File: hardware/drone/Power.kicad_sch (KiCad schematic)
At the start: 73 parts, among them Q1 ISP650P06NM, U1 STM32N645I0, U13 LM5907, U16 LMR51635XFDDCR, U18 TPS2121, U3 TPS628303, U4 TPS7A2118PQWDSGRQ1, U5 TPS628303

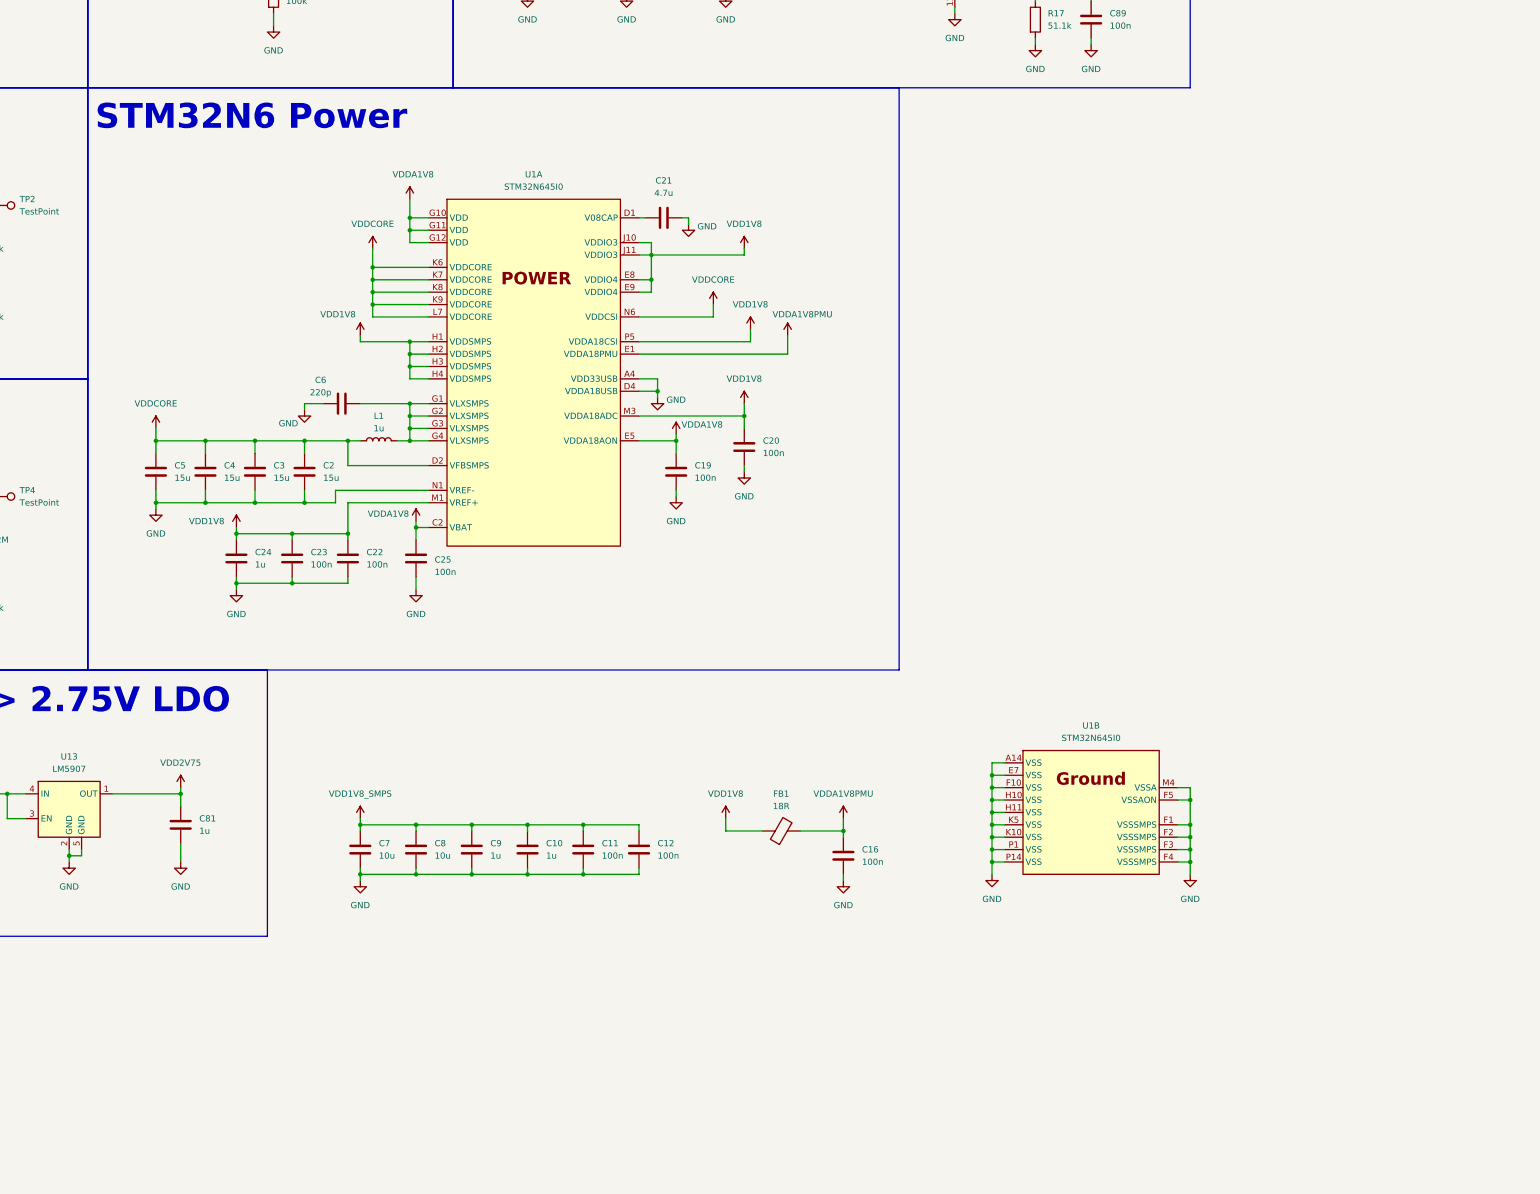
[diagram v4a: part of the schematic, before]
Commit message: Finished MCU schematic decoupling, finished system control schematic
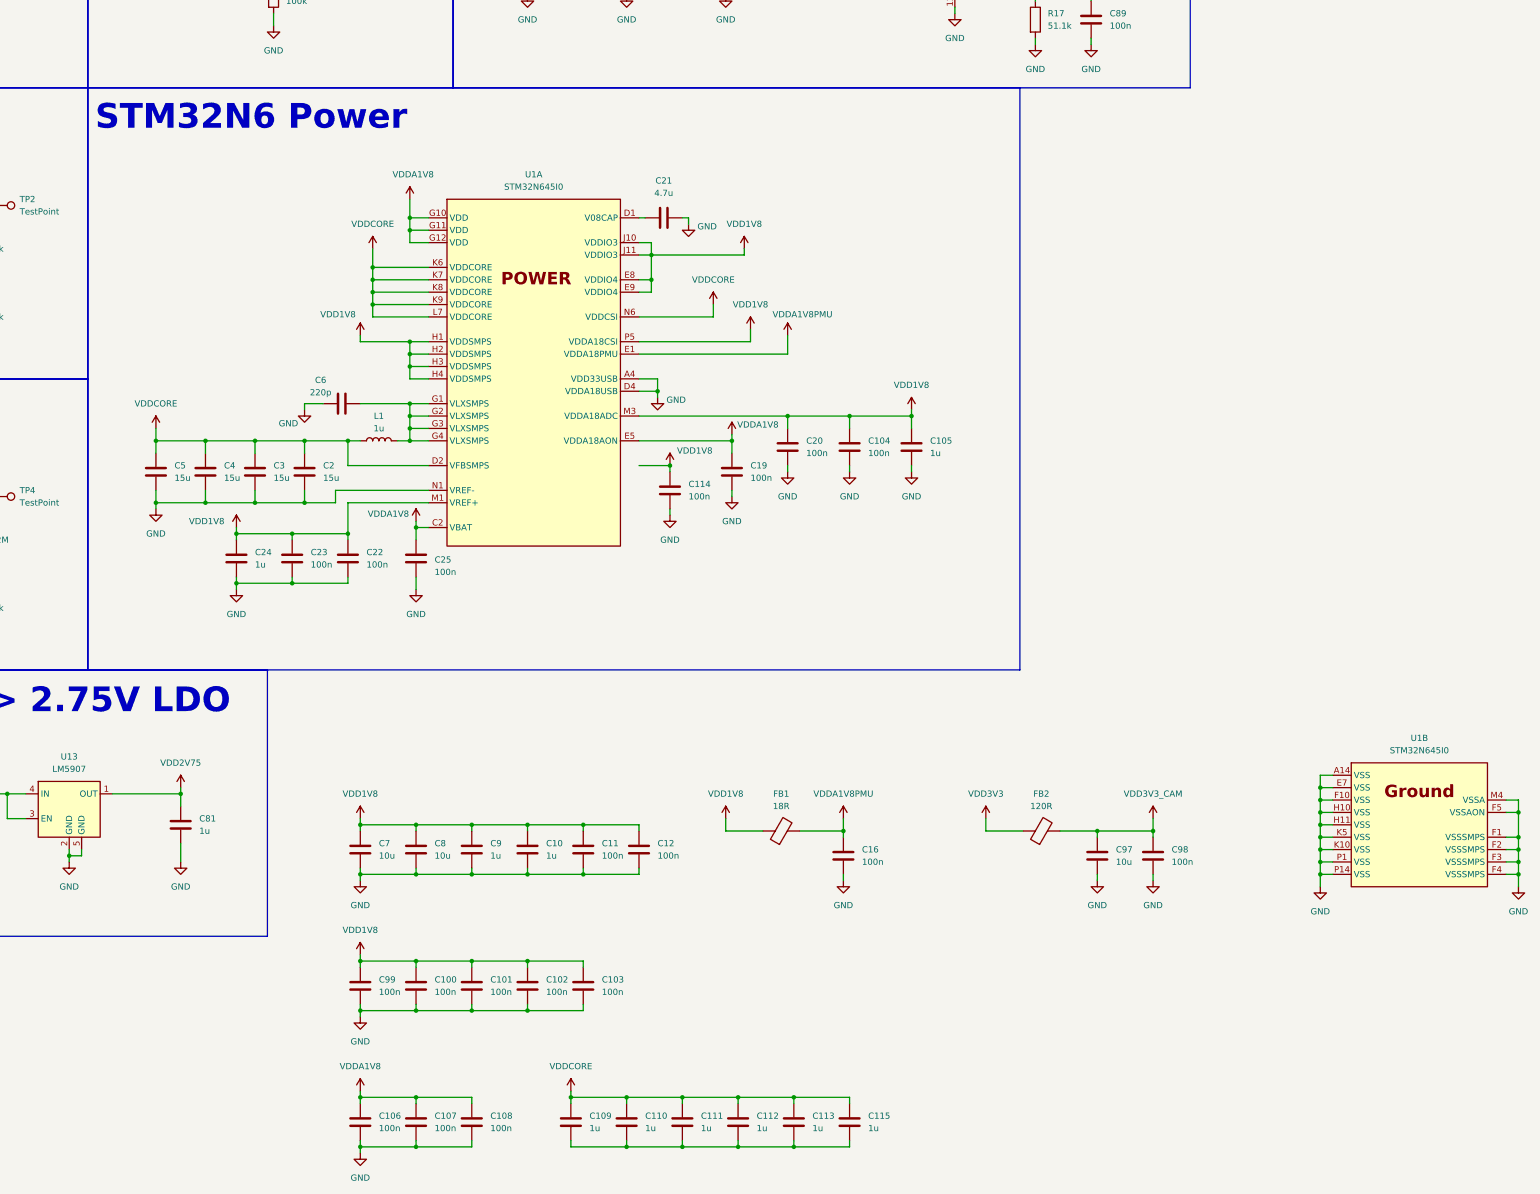
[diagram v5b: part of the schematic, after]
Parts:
- added C100, C101, C102, C103, C104, C106, C107, C108, C114, C99: 100n, symbol Device:C
- added C105, C109, C110, C111, C112, C113, C115: 1u, symbol Device:C
- added C97: 10u, Connector:Tag-Connect_TC2030-IDC-FP_2x03_P1.27mm_Vertical, symbol Device:C
- added C98: 100n, Connector:Tag-Connect_TC2030-IDC-FP_2x03_P1.27mm_Vertical, symbol Device:C
- added FB2: 120R, symbol Device:FerriteBead
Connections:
- net VDD1V8_SMPS is gone; now on net VDD1V8: C10.1, C11.1, C12.1, C7.1, C8.1, C9.1
- net GND: now also C100.2, C101.2, C102.2, C103.2, C104.2, C105.2, C106.2, C107.2, C108.2, C114.2, C97.2, C98.2, C99.2
- net VDD1V8: now also C100.1, C101.1, C102.1, C103.1, C104.1, C105.1, C114.1, C99.1
- net VDD3V3: now also FB2.1
- net VDDA1V8: now also C106.1, C107.1, C108.1
- net VDDCORE: now also C109.1, C110.1, C111.1, C112.1, C113.1, C115.1
- new net: C109.2, C110.2, C111.2, C112.2, C113.2, C115.2
- new net VDD3V3_CAM: C97.1, C98.1, FB2.2
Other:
- moved on the sheet: C19, C20, U1B

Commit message: Created pinmux table and completed pinmuxing
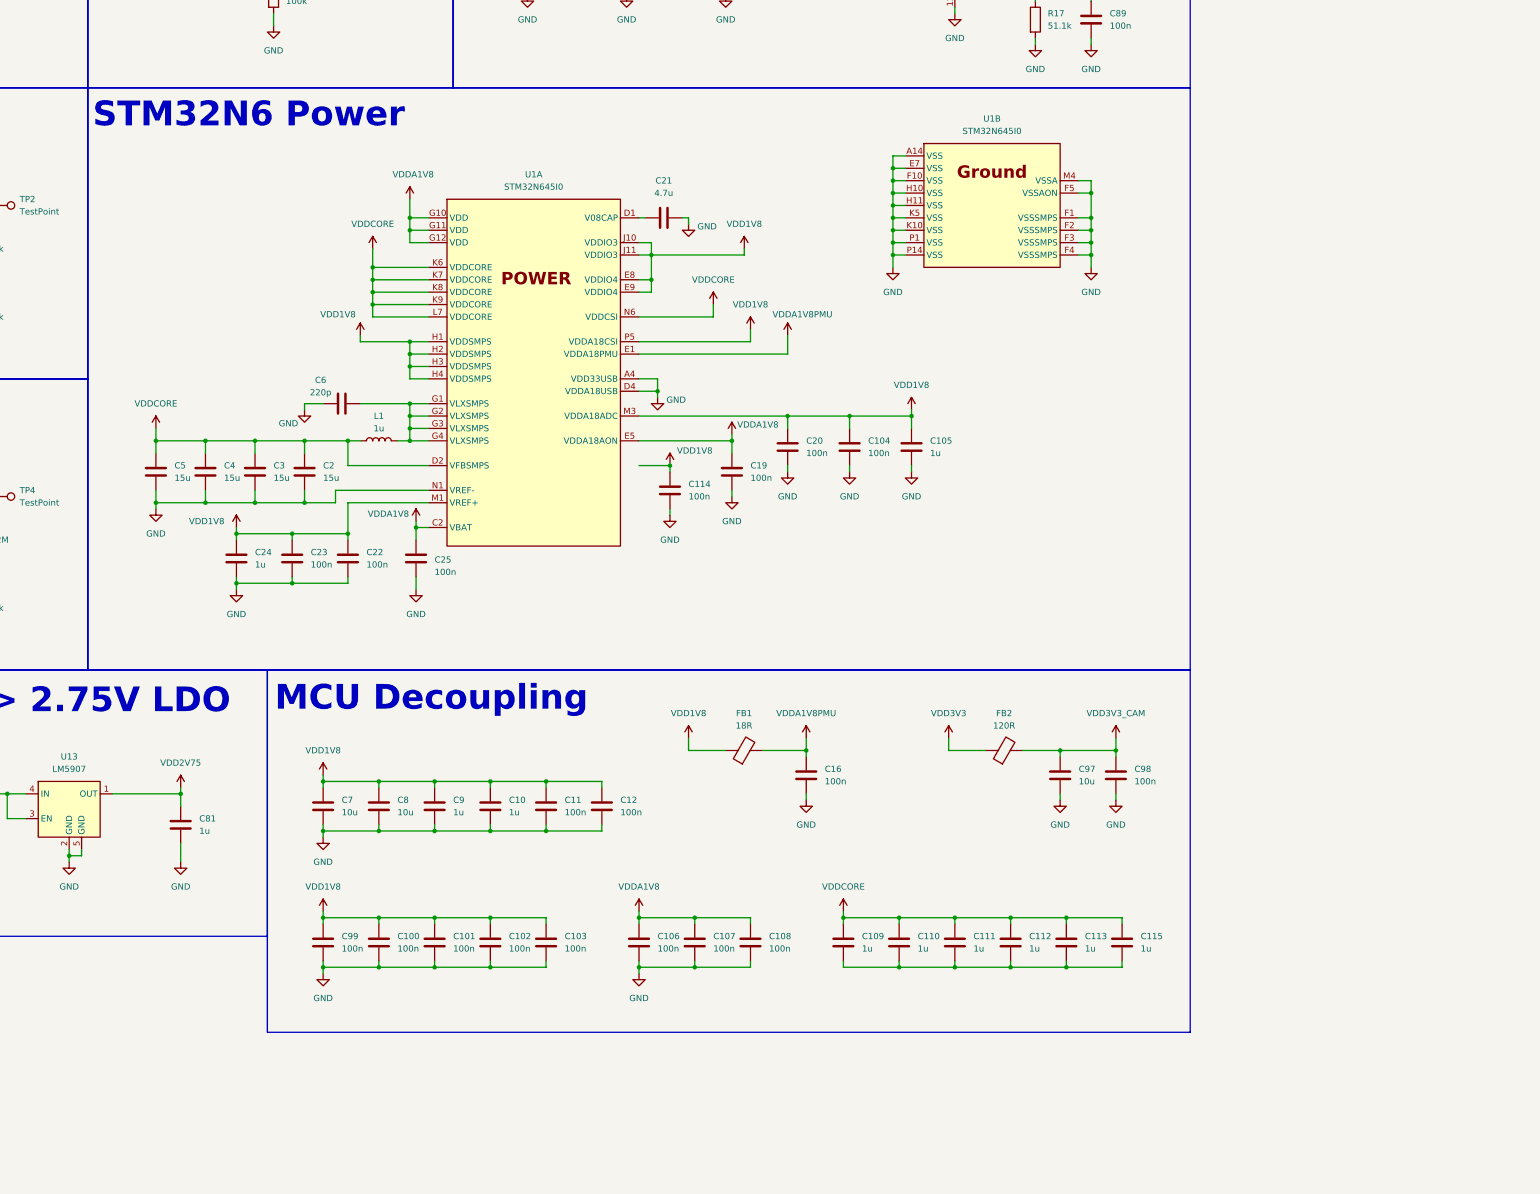
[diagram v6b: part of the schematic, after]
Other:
- note added: "MCU Decoupling"
- moved on the sheet: C10, C100, C101, C102, C103, C106, C107, C108, C109, C11, C110, C111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

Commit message: Small cleanup
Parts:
- U1: footprint (none) -> STM32N645I0:BGA178C80P14X14_1200X1200X100
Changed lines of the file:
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@@
 			)
 		)
-		(property "Footprint" ""
+		(property "Footprint" "STM32N645I0:BGA178C80P14X14_1200X1200X100"
 			(at 346.71 120.65 0)
 			(hide yes)
@@
 			)
 		)
-		(property "Footprint" ""
+		(property "Footprint" "STM32N645I0:BGA178C80P14X14_1200X1200X100"
 			(at 252.73 149.86 0)
 			(hide yes)
